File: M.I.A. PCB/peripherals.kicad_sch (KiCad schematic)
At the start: 22 parts, among them J10 Conn_01x03, J11 Conn_01x03, J12 Conn_Coaxial, J3 Conn_01x03, J4 Conn_01x03, J5 Conn_01x03, J6 Conn_01x03, J7 MSD-4-A, J8 Conn_01x03, J9 Conn_01x03, U15 74AHC541, U16 RFM95W-915S2

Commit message: Worked on Layout, Changed IMU
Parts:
- added D3, D4, D5, D6: BZT52Bxx, Diode_SMD:D_SOD-123F, symbol Diode:BZT52Bxx
- added F1, F2, F3, F4: ERBRE3R00V, JLCImport:ERBRE3R00V, symbol JLCImport:ERBRE3R00V
- added J13, J15, J16, J17: Screw_Terminal_01x02, TerminalBlock_Phoenix:TerminalBlock_Phoenix_MKDS-1-2-3.81_1x02_P3.81mm_Horizontal, symbol Connector:Screw_Terminal_01x02
- added Q1, Q2, Q3, Q4: AO3400A, Package_TO_SOT_SMD:SOT-23, symbol Transistor_FET:AO3400A
- added R34, R39, R43, R47: 1k, Resistor_SMD:R_0603_1608Metric, symbol Device:R
- added R35, R40, R44, R48: 10k, Resistor_SMD:R_0603_1608Metric, symbol Device:R
- added R36, R38, R42, R46: 5M, Resistor_SMD:R_0603_1608Metric, symbol Device:R
- added R37, R41, R45, R49: 1M, Resistor_SMD:R_0603_1608Metric, symbol Device:R
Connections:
- net GND: now also D3.2 (A), D4.2 (A), D5.2 (A), D6.2 (A), Q1.2 (S), Q2.2 (S), Q3.2 (S), Q4.2 (S), R35.1, R37.2, R40.1, R41.2, R44.1, R45.2, R48.1, R49.2
- new net: D5.1 (K), Q3.1 (G), R43.2, R44.2
- new net: F1.1, J13.2 (Pin_2)
- new net: D4.1 (K), Q1.1 (G), R34.2, R35.2
- new net: D3.1 (K), Q2.1 (G), R39.2, R40.2
- new net: D6.1 (K), Q4.1 (G), R47.2, R48.2
- new net: J15.1 (Pin_1), Q2.3 (D), R38.1
- new net: J16.1 (Pin_1), Q3.3 (D), R42.1
- new net: J17.1 (Pin_1), Q4.3 (D), R46.1
- new net: F4.1, J17.2 (Pin_2)
- new net: F3.1, J16.2 (Pin_2)
- new net: F2.1, J15.2 (Pin_2)
- new net: J13.1 (Pin_1), Q1.3 (D), R36.1
- new net Cont_Sense1: R36.2, R37.1
- new net Cont_Sense2: R38.2, R41.1
- new net Cont_Sense3: R42.2, R45.1
- new net Cont_Sense4: R46.2, R49.1
- new net IGN_1: R34.1
- new net IGN_2: R39.1
- new net IGN_3: R43.1
- new net IGN_4: R47.1
- new net V_IGN: F1.2, F2.2, F3.2, F4.2

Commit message: added servo pin protector and changed screw terminal size
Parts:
- J13, J15, J16, J17: footprint TerminalBlock_Phoenix:TerminalBlock_Phoenix_MKDS-1-2-3.81_1x02_P3.81mm_Horizontal -> TerminalBlock_Phoenix:TerminalBlock_Phoenix_PT-1,5-2-3.5-H_1x02_P3.50mm_Horizontal
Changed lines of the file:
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@@
 			)
 		)
-		(property "Footprint" "TerminalBlock_Phoenix:TerminalBlock_Phoenix_MKDS-1-2-3.81_1x02_P3.81mm_Horizontal"
+		(property "Footprint" "TerminalBlock_Phoenix:TerminalBlock_Phoenix_PT-1,5-2-3.5-H_1x02_P3.50mm_Horizontal"
 			(at 107.95 161.29 0)
 			(effects
@@
 			)
 		)
-		(property "Footprint" "TerminalBlock_Phoenix:TerminalBlock_Phoenix_MKDS-1-2-3.81_1x02_P3.81mm_Horizontal"
+		(property "Footprint" "TerminalBlock_Phoenix:TerminalBlock_Phoenix_PT-1,5-2-3.5-H_1x02_P3.50mm_Horizontal"
 			(at 41.91 161.29 0)
 			(effects
@@
 			)
 		)
-		(property "Footprint" "TerminalBlock_Phoenix:TerminalBlock_Phoenix_MKDS-1-2-3.81_1x02_P3.81mm_Horizontal"
+		(property "Footprint" "TerminalBlock_Phoenix:TerminalBlock_Phoenix_PT-1,5-2-3.5-H_1x02_P3.50mm_Horizontal"
 			(at 41.91 127 0)
 			(effects
@@
 			)
 		)
-		(property "Footprint" "TerminalBlock_Phoenix:TerminalBlock_Phoenix_MKDS-1-2-3.81_1x02_P3.81mm_Horizontal"
+		(property "Footprint" "TerminalBlock_Phoenix:TerminalBlock_Phoenix_PT-1,5-2-3.5-H_1x02_P3.50mm_Horizontal"
 			(at 107.95 127 0)
 			(effects

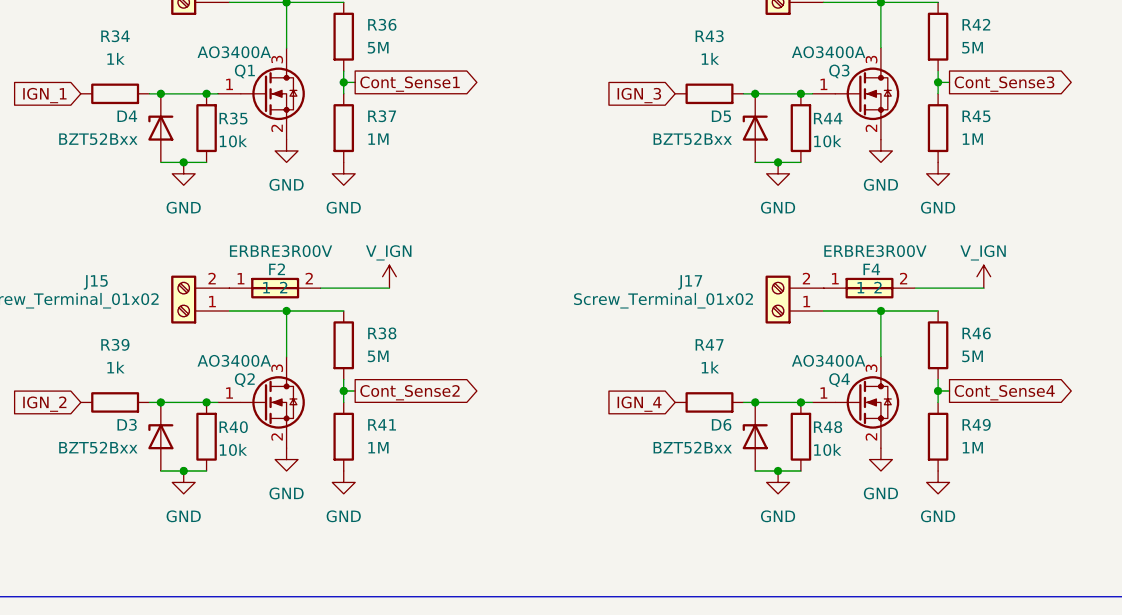
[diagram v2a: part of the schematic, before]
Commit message: updated LDO and Power Sensor
may need to change LDO to support power draw of RFM95CW
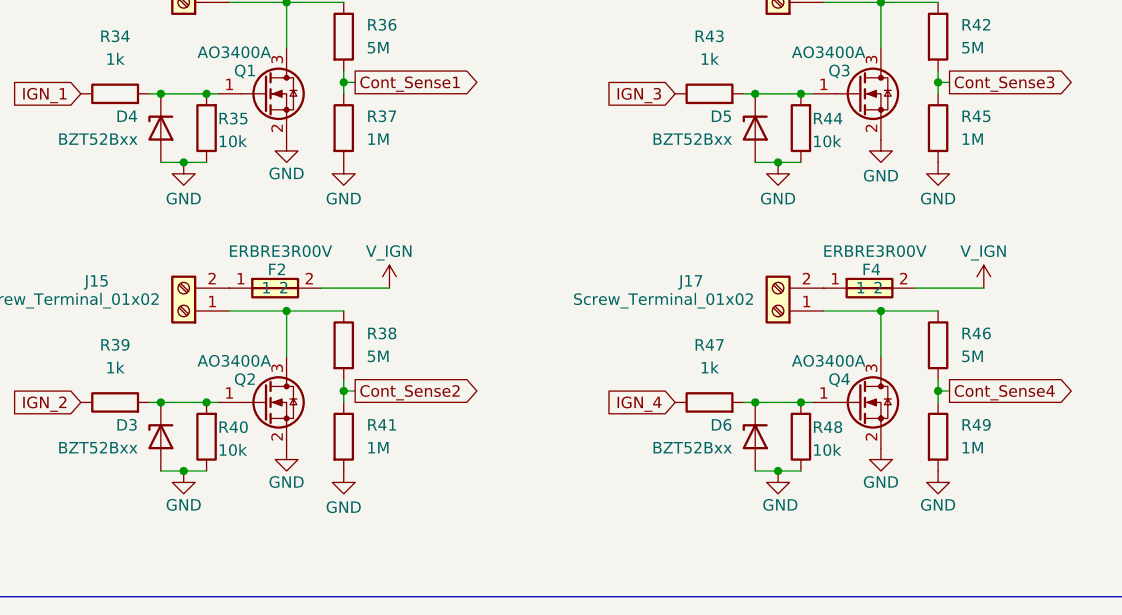
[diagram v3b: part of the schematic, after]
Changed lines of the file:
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@@
 		(on_board yes)
 		(dnp no)
-		(fields_autoplaced yes)
 		(property "Reference" "#PWR0125"
 			(at 107.95 151.13 0)
@@
 		)
 		(property "Value" "GND"
-			(at 107.95 149.86 0)
+			(at 107.95 148.844 0)
 			(effects
 				(font
@@
 		(on_board yes)
 		(dnp no)
-		(fields_autoplaced yes)
 		(property "Reference" "#PWR0122"
 			(at 59.69 185.42 0)
@@
 		)
 		(property "Value" "GND"
-			(at 59.69 184.15 0)
+			(at 59.69 183.134 0)
 			(effects
 				(font
@@
 		(on_board yes)
 		(dnp no)
-		(fields_autoplaced yes)
 		(property "Reference" "#PWR0121"
 			(at 41.91 185.42 0)
@@
 		)
 		(property "Value" "GND"
-			(at 41.91 184.15 0)
+			(at 41.91 182.88 0)
 			(effects
 				(font
@@
 		(on_board yes)
 		(dnp no)
-		(fields_autoplaced yes)
 		(property "Reference" "#PWR0116"
 			(at 59.69 151.13 0)
@@
 		)
 		(property "Value" "GND"
-			(at 59.69 149.86 0)
+			(at 59.69 148.844 0)
 			(effects
 				(font
@@
 		(on_board yes)
 		(dnp no)
-		(fields_autoplaced yes)
 		(property "Reference" "#PWR0120"
 			(at 53.34 182.88 0)
@@
 		)
 		(property "Value" "GND"
-			(at 53.34 181.61 0)
+			(at 53.34 180.34 0)
 			(effects
 				(font
@@
 		(on_board yes)
 		(dnp no)
-		(fields_autoplaced yes)
 		(property "Reference" "#PWR0124"
 			(at 119.38 148.59 0)
@@
 		)
 		(property "Value" "GND"
-			(at 119.38 147.32 0)
+			(at 119.38 146.304 0)
 			(effects
 				(font
@@
 		(on_board yes)
 		(dnp no)
-		(fields_autoplaced yes)
 		(property "Reference" "#PWR0130"
 			(at 125.73 185.42 0)
@@
 		)
 		(property "Value" "GND"
-			(at 125.73 184.15 0)
+			(at 125.73 182.88 0)
 			(effects
 				(font
@@
 		(on_board yes)
 		(dnp no)
-		(fields_autoplaced yes)
 		(property "Reference" "#PWR0129"
 			(at 107.95 185.42 0)
@@
 		)
 		(property "Value" "GND"
-			(at 107.95 184.15 0)
+			(at 108.204 182.88 0)
 			(effects
 				(font
@@
 		(on_board yes)
 		(dnp no)
-		(fields_autoplaced yes)
 		(property "Reference" "#PWR0126"
 			(at 125.73 151.13 0)
@@
 		)
 		(property "Value" "GND"
-			(at 125.73 149.86 0)
+			(at 125.73 148.844 0)
 			(effects
 				(font
@@
 		(on_board yes)
 		(dnp no)
-		(fields_autoplaced yes)
 		(property "Reference" "#PWR0128"
 			(at 119.38 182.88 0)
@@
 		)
 		(property "Value" "GND"
-			(at 119.38 181.61 0)
+			(at 119.38 180.34 0)
 			(effects
 				(font
@@
 		(on_board yes)
 		(dnp no)
-		(fields_autoplaced yes)
 		(property "Reference" "#PWR0114"
 			(at 41.91 151.13 0)
@@
 		)
 		(property "Value" "GND"
-			(at 41.91 149.86 0)
+			(at 41.91 148.844 0)
 			(effects
 				(font
@@
 		(on_board yes)
 		(dnp no)
-		(fields_autoplaced yes)
 		(property "Reference" "#PWR0115"
 			(at 53.34 148.59 0)
@@
 		)
 		(property "Value" "GND"
-			(at 53.34 147.32 0)
+			(at 53.34 146.05 0)
 			(effects
 				(font

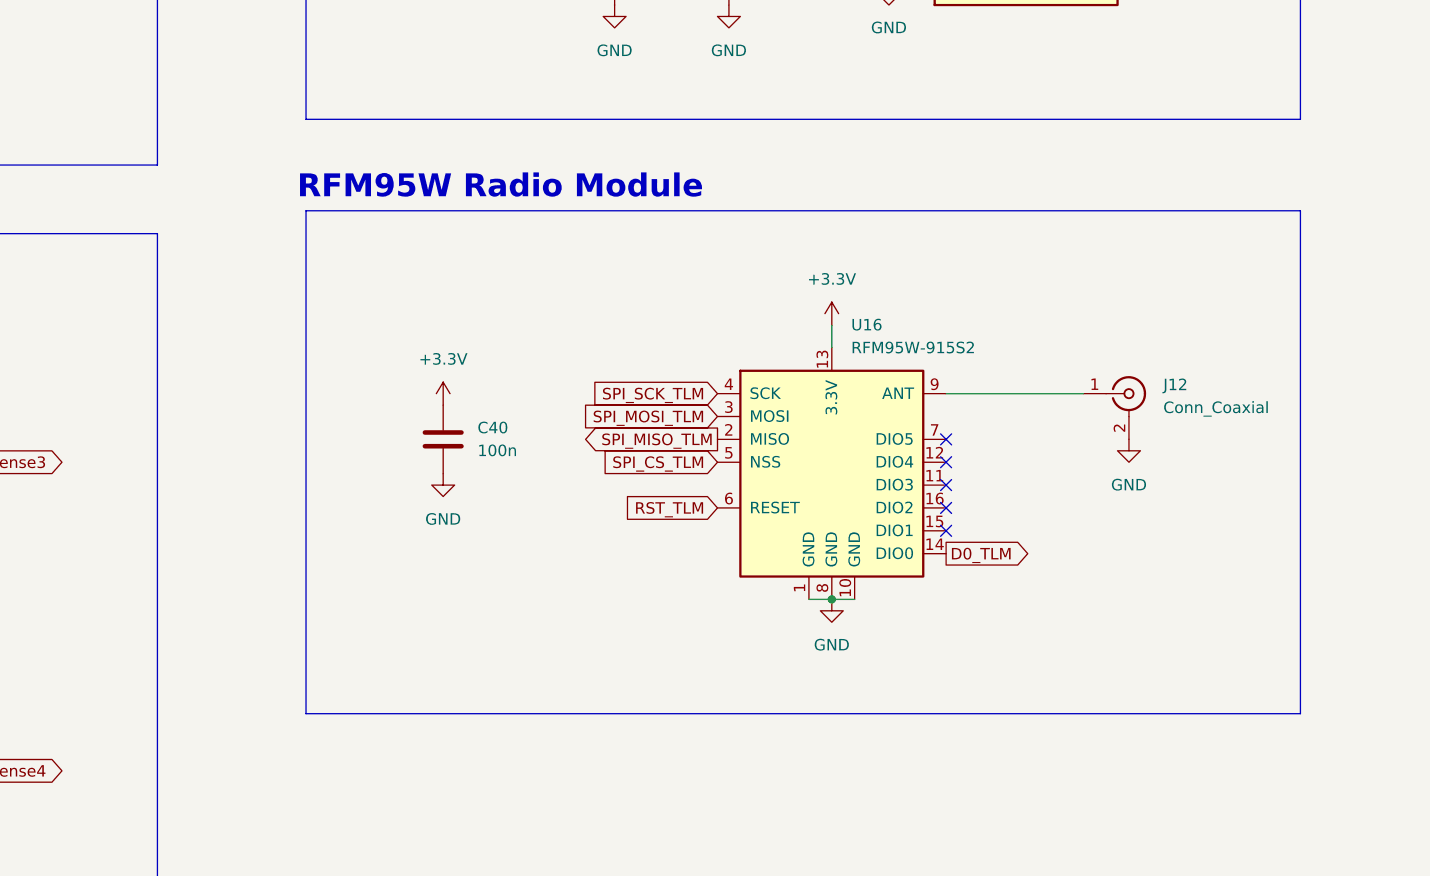
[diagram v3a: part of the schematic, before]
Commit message: Finished Layout other than gps, extra connectors, and ignition lines
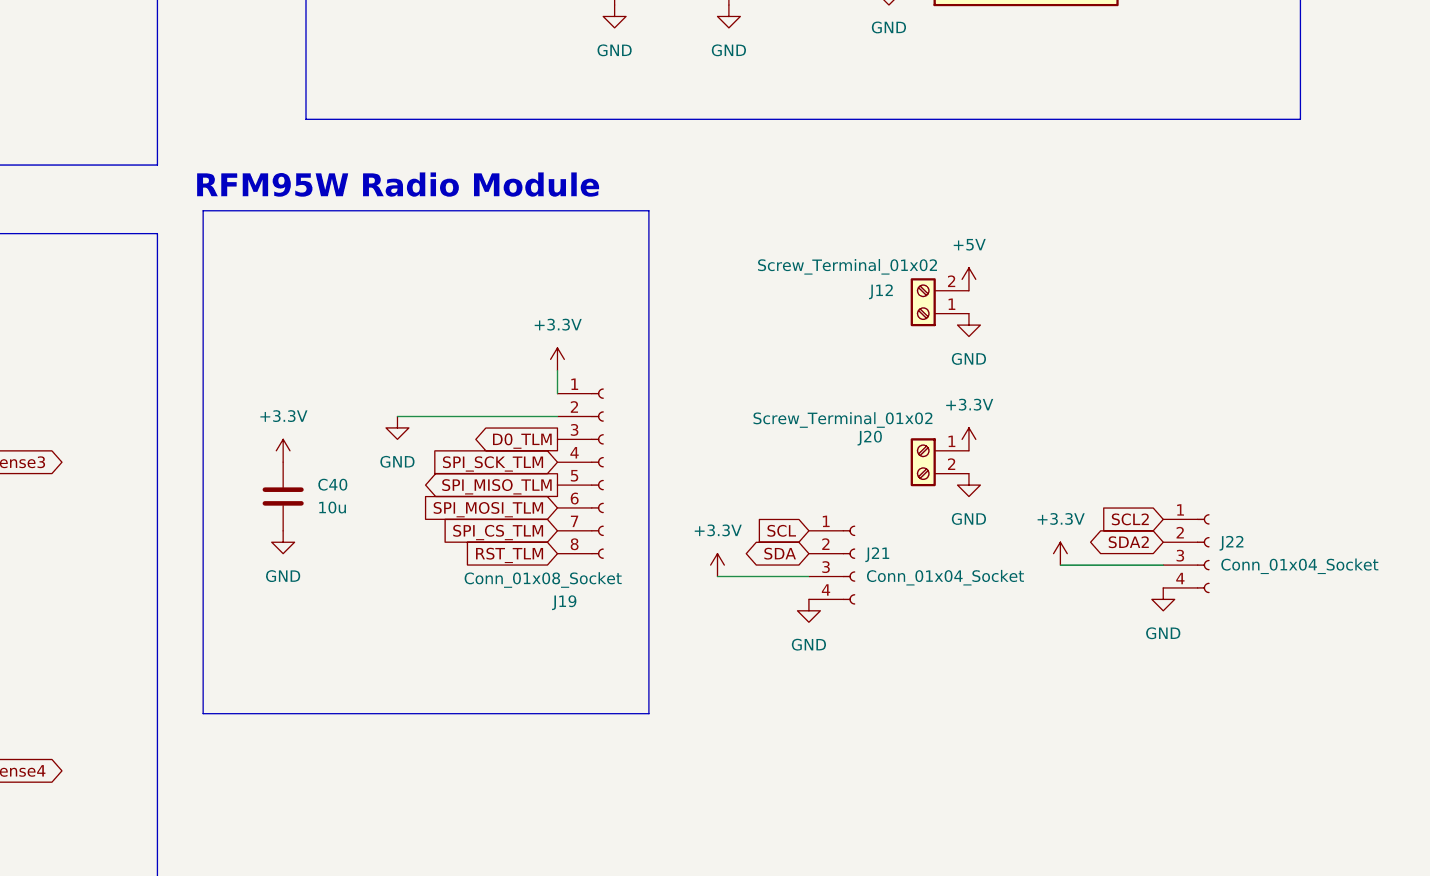
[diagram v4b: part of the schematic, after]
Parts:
- removed J12: Conn_Coaxial, Connector_Coaxial:SMA_Amphenol_901-144_Vertical, symbol Connector:Conn_Coaxial
- removed U16: RFM95W-915S2, RF_Module:HOPERF_RFM9XW_SMD, symbol RF_Module:RFM95W-915S2
- added J12, J20: Screw_Terminal_01x02, TerminalBlock_Phoenix:TerminalBlock_Phoenix_PT-1,5-2-3.5-H_1x02_P3.50mm_Horizontal, symbol Connector:Screw_Terminal_01x02
- added J19: Conn_01x08_Socket, Connector_JST:JST_SHL_SM08B-SHLS-TF_1x08-1MP_P1.00mm_Horizontal, symbol Connector:Conn_01x08_Socket
- added J21, J22: Conn_01x04_Socket, Connector_JST:JST_PH_B4B-PH-K_1x04_P2.00mm_Vertical, symbol Connector:Conn_01x04_Socket
- C40: value 100n -> 10u; footprint Capacitor_SMD:C_0603_1608Metric -> Capacitor_SMD:C_0805_2012Metric; LCSC Part Number C1525 -> (none)
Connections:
- net +3.3V: now also J19.1 (Pin_1), J20.1 (Pin_1), J21.3 (Pin_3), J22.3 (Pin_3)
- net +5V: now also J12.2 (Pin_2)
- net D0_TLM: now also J19.3 (Pin_3)
- net GND: now also J12.1 (Pin_1), J19.2 (Pin_2), J20.2 (Pin_2), J21.4 (Pin_4), J22.4 (Pin_4)
- net RST_TLM: now also J19.8 (Pin_8)
- net SPI_CS_TLM: now also J19.7 (Pin_7)
- net SPI_MISO_TLM: now also J19.5 (Pin_5)
- net SPI_MOSI_TLM: now also J19.6 (Pin_6)
- net SPI_SCK_TLM: now also J19.4 (Pin_4)
- new net SCL: J21.1 (Pin_1)
- new net SCL2: J22.1 (Pin_1)
- new net SDA: J21.2 (Pin_2)
- new net SDA2: J22.2 (Pin_2)
- no-connect marks 5 -> 0

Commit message: Worked More on Layout/Wiring
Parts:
- added J23: Conn_01x04_Socket, Connector_JST:JST_PH_B4B-PH-K_1x04_P2.00mm_Vertical, symbol Connector:Conn_01x04_Socket
- J12, J13, J15, J16, J17, J20: footprint TerminalBlock_Phoenix:TerminalBlock_Phoenix_PT-1,5-2-3.5-H_1x02_P3.50mm_Horizontal -> PCM_SparkFun-Connector:ScrewTerminal_1x02_P3.5mm_Horizontal_Black
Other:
- moved on the sheet: J12, J20, J21, J22

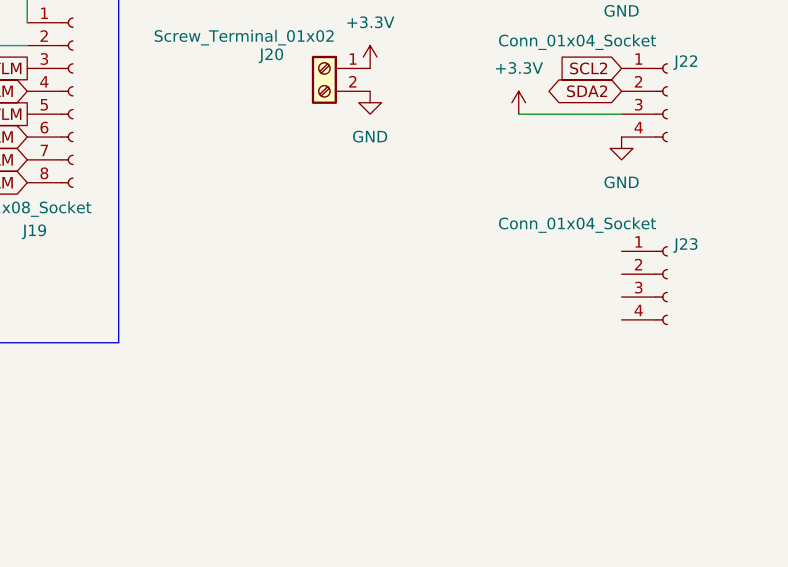
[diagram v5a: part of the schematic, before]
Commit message: Wired Sensors
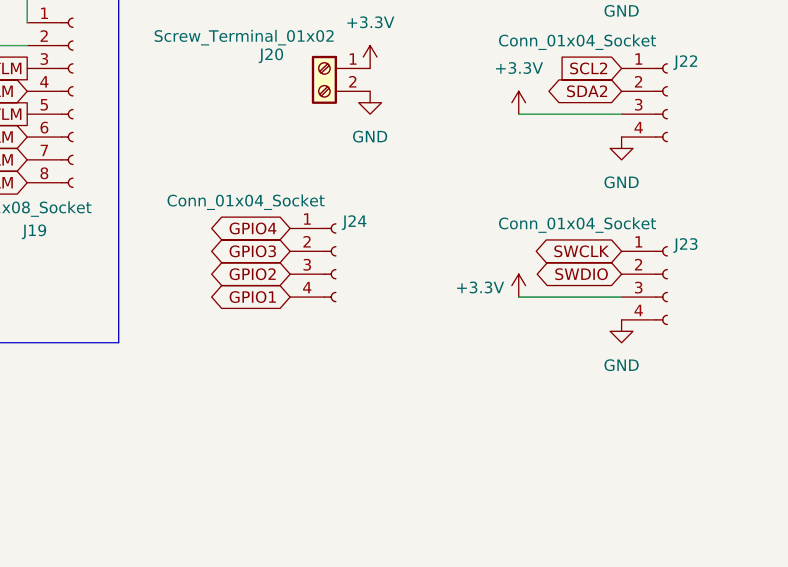
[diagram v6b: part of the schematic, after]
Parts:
- added J24: Conn_01x04_Socket, Connector_JST:JST_PH_B4B-PH-K_1x04_P2.00mm_Vertical, symbol Connector:Conn_01x04_Socket
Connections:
- net +3.3V: now also J23.3 (Pin_3)
- net GND: now also J23.4 (Pin_4)
- net SWCLK: now reaches J23.1 (Pin_1)
- net SWDIO: now reaches J23.2 (Pin_2)
- new net GPIO1: J24.4 (Pin_4)
- new net GPIO2: J24.3 (Pin_3)
- new net GPIO3: J24.2 (Pin_2)
- new net GPIO4: J24.1 (Pin_1)
